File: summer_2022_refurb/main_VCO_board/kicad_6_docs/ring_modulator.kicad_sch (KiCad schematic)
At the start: 1 part

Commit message: Main VCO progress
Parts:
- SW?: value SW_SPDT_MSM -> SW_SPDT_CO
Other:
- title: (none) -> Josh Ox Ribon Synth Main VCO board
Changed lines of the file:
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@@
 (kicad_sch (version 20211123) (generator eeschema)
   (paper "A4")
+  (title_block
+    (title "Josh Ox Ribon Synth Main VCO board")
+    (date "2022-06-18")
+    (rev "0")
+    (comment 2 "creativecommons.org/licences/by/4.0")
+    (comment 3 "license: CC by 4.0")
+    (comment 4 "Author: Jordan Acete")
+  )
   (junction (at 128.27 73.66) (diameter 0) (color 0 0 0 0)
   )
@@
     (in_bom yes) (on_board yes) (fields_autoplaced)
     (property "Reference" "SW?" (id 0) (at 175.133 68.58 0))
-    (property "Value" "SW_SPDT_MSM" (id 1) (at 175.133 71.12 0))
+    (property "Value" "SW_SPDT_CO" (id 1) (at 175.133 71.12 0))
     (property "Footprint" "" (id 2) (at 175.26 76.2 0)
       (effects (font (size 1.27 1.27)) hide)

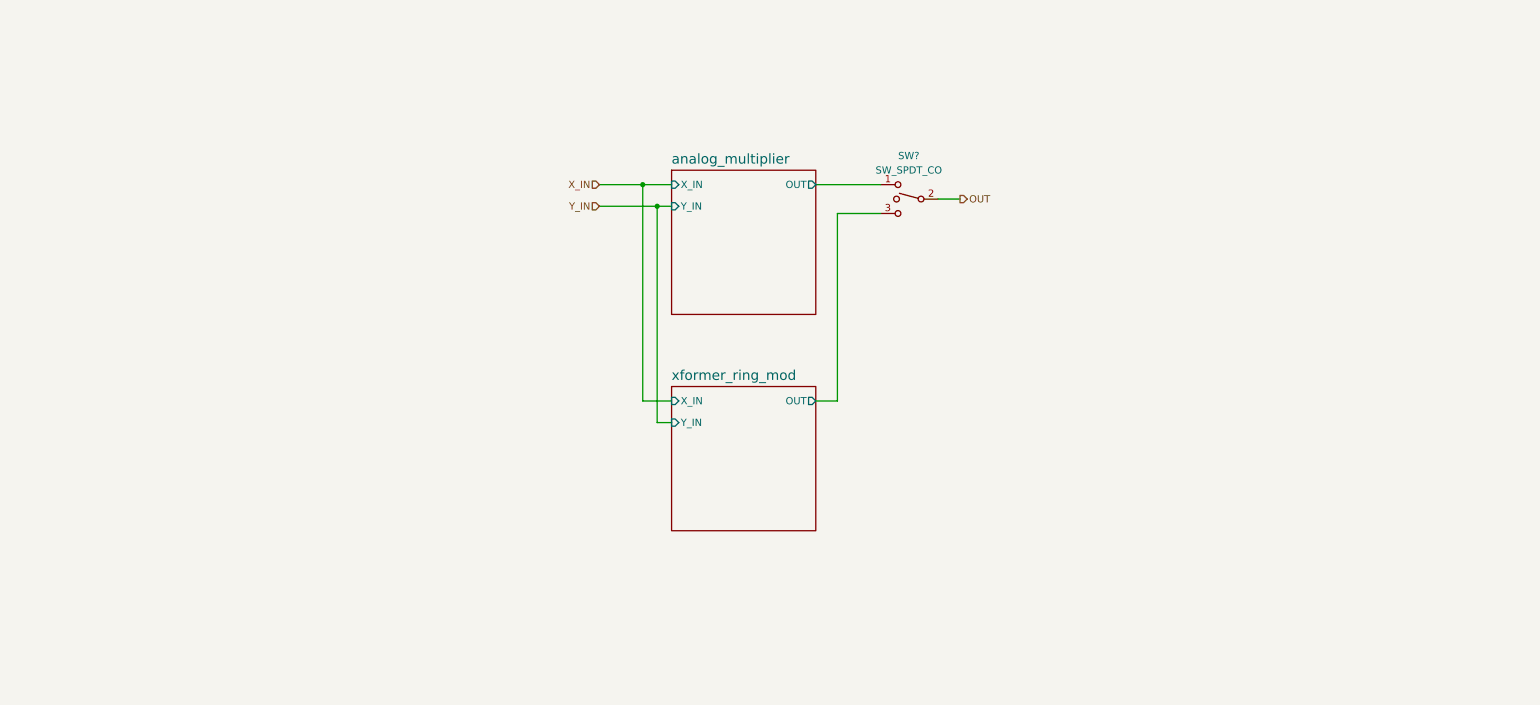
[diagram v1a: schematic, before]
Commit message: Progress on main VCO, schem getting close but not done
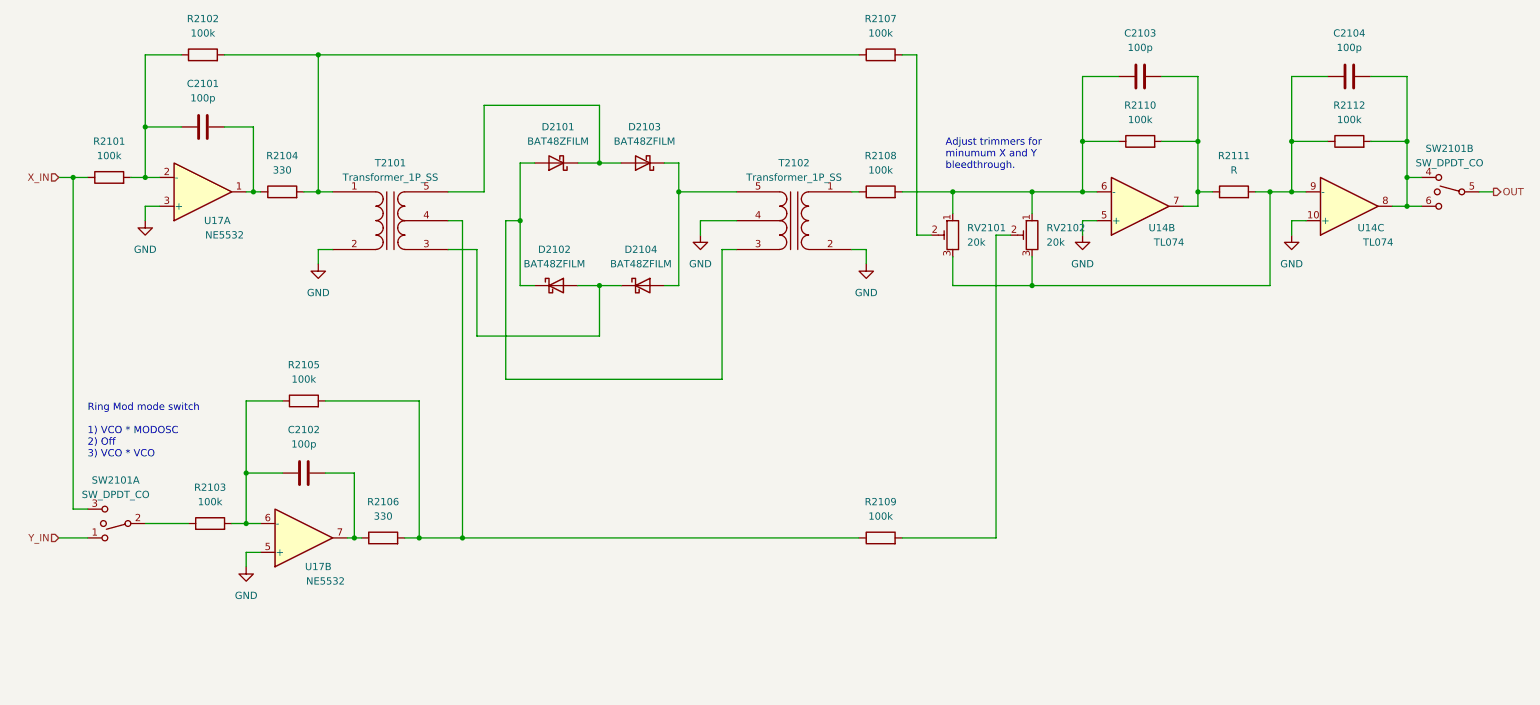
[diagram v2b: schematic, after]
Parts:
- removed SW?: SW_SPDT_CO, symbol Switch:SW_SPDT_MSM
- added C2101, C2102, C2103, C2104: 100p, symbol Device:C
- added D2101, D2102, D2103, D2104: BAT48ZFILM, Diode_SMD:D_SOD-123, symbol Diode:BAT48ZFILM
- added R2101, R2102, R2103, R2105, R2107, R2108, R2109, R2110, R2112: 100k, symbol Device:R
- added R2104, R2106: 330, symbol Device:R
- added R2111: R, symbol Device:R
- added RV2101, RV2102: 20k, symbol Device:R_Potentiometer_Trim
- added SW2101: SW_DPDT_CO, symbol custom_symbols:SW_DPDT_CO
- added T2101, T2102: Transformer_1P_SS, symbol Device:Transformer_1P_SS
- added U14: TL074, symbol Amplifier_Operational:TL074
- added U17: NE5532, symbol Amplifier_Operational:NE5532
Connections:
- net OUT: now also SW2101.5
- net X_IN: now also R2101.1, SW2101.3
- net Y_IN: now also SW2101.1
- new net: D2101.1 (K), D2103.2 (A), T2101.5 (SB)
- new net: D2101.2 (A), D2102.1 (K), T2102.3 (SA)
- new net: C2101.2, R2104.1, U17.1
- new net: R2102.2, R2104.2, R2107.1, T2101.1 (AA)
- new net: R2107.2, RV2101.2
- new net: C2102.2, R2106.1, U17.7
- new net: R2105.2, R2106.2, R2109.1, T2101.4 (SC)
- new net: C2104.1, R2111.2, R2112.1, RV2101.3, RV2102.3, U14.9 (-)
- new net: C2104.2, R2112.2, SW2101.4, SW2101.6, U14.8
- new net: D2102.2 (A), D2104.1 (K), T2101.3 (SA)
- new net: C2102.1, R2103.2, R2105.1, U17.6 (-)
- new net: C2101.1, R2101.2, R2102.1, U17.2 (-)
- new net: D2103.1 (K), D2104.2 (A), T2102.5 (SB)
- new net: C2103.1, R2108.2, R2110.1, RV2101.1, RV2102.1, U14.6 (-)
- new net: R2103.1, SW2101.2
- new net: C2103.2, R2110.2, R2111.1, U14.7
- new net: R2108.1, T2102.1 (AA)
- new net: R2109.2, RV2102.2
- new net GND: T2101.2 (AB), T2102.2 (AB), T2102.4 (SC), U14.10 (+), U14.5 (+), U17.3 (+), U17.5 (+)
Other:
- removed sheet analog_multiplier
- removed sheet xformer_ring_mod
- note added: "Adjust trimmers for minumum X and Y bleedthrough."
- note added: "Ring Mod mode switch 1) VCO * MODOSC 2) Off 3) VCO * VCO"

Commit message: Main VCO rough parts placement
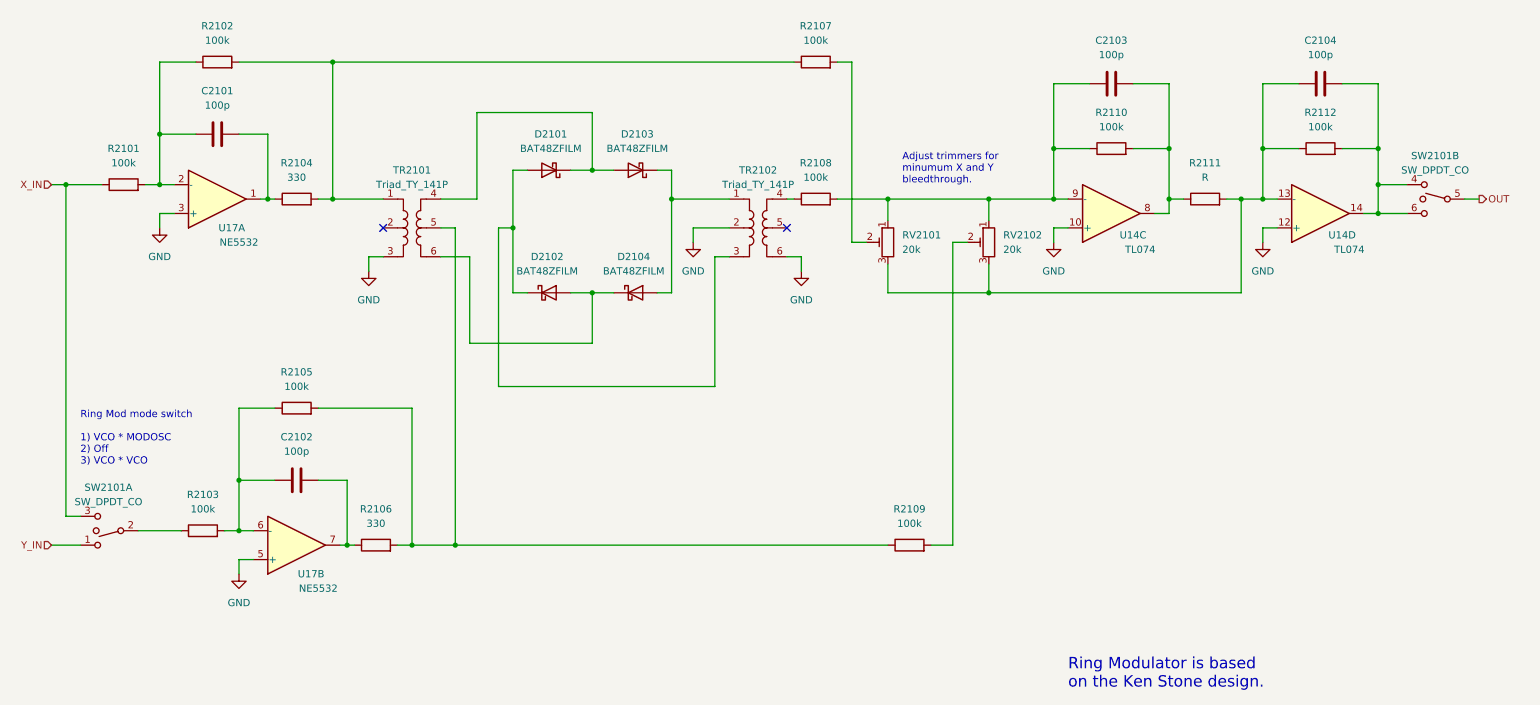
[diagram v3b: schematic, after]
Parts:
- removed T2101, T2102: Transformer_1P_SS, symbol Device:Transformer_1P_SS
- added TR2101, TR2102: Triad_TY_141P, custom_footprints:Triad_TY-141P, symbol custom_symbols:Triad_TY_141P
- C2101, C2102, C2103, C2104: footprint (none) -> Capacitor_SMD:C_0805_2012Metric
- R2101, R2102, R2103, R2104, R2105, R2106, R2107, R2108, R2109, R2110, R2111, R2112: footprint (none) -> Resistor_SMD:R_0805_2012Metric
- RV2101, RV2102: footprint (none) -> Potentiometer_THT:Potentiometer_Bourns_3296W_Vertical
- SW2101: footprint (none) -> custom_footprints:DPDT_mini_toggle
- U14: footprint (none) -> Package_SO:SOIC-14_3.9x8.7mm_P1.27mm
- U17: footprint (none) -> Package_SO:SOIC-8_3.9x4.9mm_P1.27mm
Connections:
- net GND: now also U14.10 (+), U14.12 (+), TR2101.3, TR2102.2, TR2102.6; no longer U14.10 (+), U14.5 (+)
- net at D2101.1 (K), D2103.2 (A): now also TR2101.4
- net at D2101.2 (A), D2102.1 (K): now also TR2102.3
- net at R2102.2, R2104.2, R2107.1: now also TR2101.1
- net at R2105.2, R2106.2, R2109.1: now also TR2101.5
- net at C2104.1, R2111.2, R2112.1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: now also U14.13 (-); no longer U14.9 (-)
- net at C2104.2, R2112.2, SW2101.4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: now also U14.14; no longer U14.8
- net at D2102.2 (A), D2104.1 (K): now also TR2101.6
- net at D2103.1 (K), D2104.2 (A): now also TR2102.1
- net at C2103.1, R2108.2, R2110.1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: now also U14.9 (-); no longer U14.6 (-)
- net at C2103.2, R2110.2, R2111.1: now also U14.8; no longer U14.7
- net at R2108.1: now also TR2102.4
- no-connect marks 0 -> 2
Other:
- note added: "Ring Modulator is based on the Ken Stone design."
- moved on the sheet: C2101, C2102, C2103, C2104, D2101, D2102, D2103, D2104, R2101, R2102, R2103, R2104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

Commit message: Begin VCO pcb layout
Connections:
- net GND: now also U14.3 (+), U14.5 (+); no longer U14.10 (+), U14.12 (+)
- net at C2104.1, R2111.2, R2112.1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: now also U14.2 (-); no longer U14.13 (-)
- net at C2104.2, R2112.2, SW2101.4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: now also U14.1; no longer U14.14
- net at C2103.1, R2108.2, R2110.1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: now also U14.6 (-); no longer U14.9 (-)
- net at C2103.2, R2110.2, R2111.1: now also U14.7; no longer U14.8
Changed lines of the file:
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@@
     (pin "2")
   )
-  (symbol (lib_id "Amplifier_Operational:TL074") (at 247.65 78.74 0) (mirror x) (unit 4)
+  (symbol (lib_id "Amplifier_Operational:TL074") (at 247.65 78.74 0) (mirror x) (unit 1)
     (in_bom yes) (on_board yes)
     (property "Reference" "U14" (id 0) (at 251.46 82.55 0))
@@
     (pin "2")
   )
-  (symbol (lib_id "Amplifier_Operational:TL074") (at 210.82 78.74 0) (mirror x) (unit 3)
+  (symbol (lib_id "Amplifier_Operational:TL074") (at 210.82 78.74 0) (mirror x) (unit 2)
     (in_bom yes) (on_board yes)
     (property "Reference" "U14" (id 0) (at 214.63 82.55 0))
